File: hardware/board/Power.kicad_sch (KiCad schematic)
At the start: 34 parts

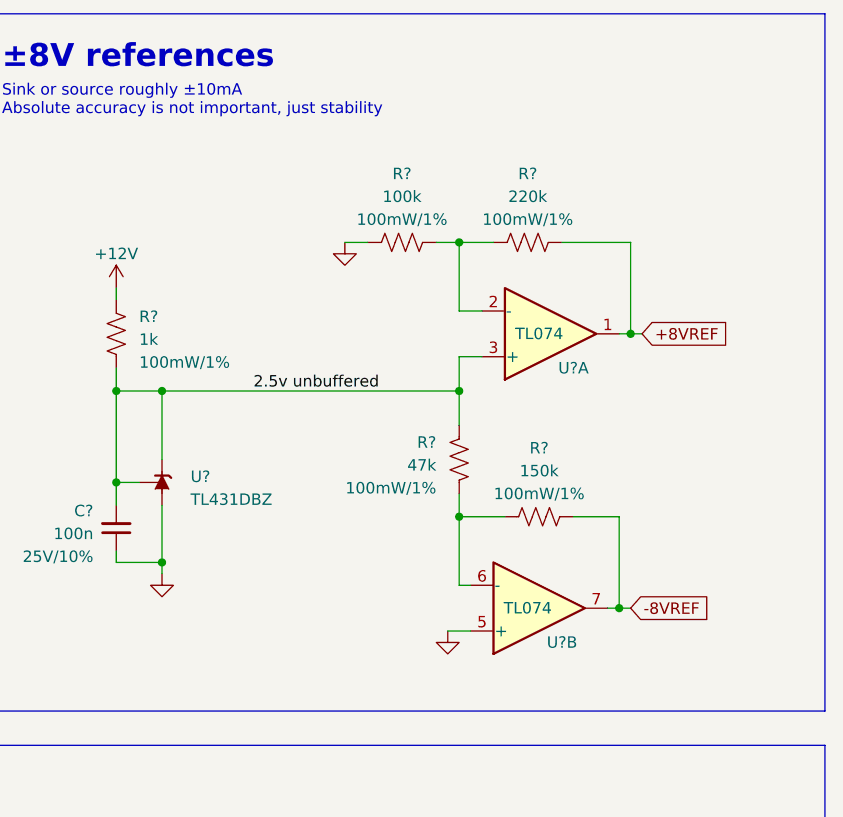
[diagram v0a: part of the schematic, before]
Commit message: Schematic getting closer to being finished
Schematic should be close to being ready to assign MPNs.
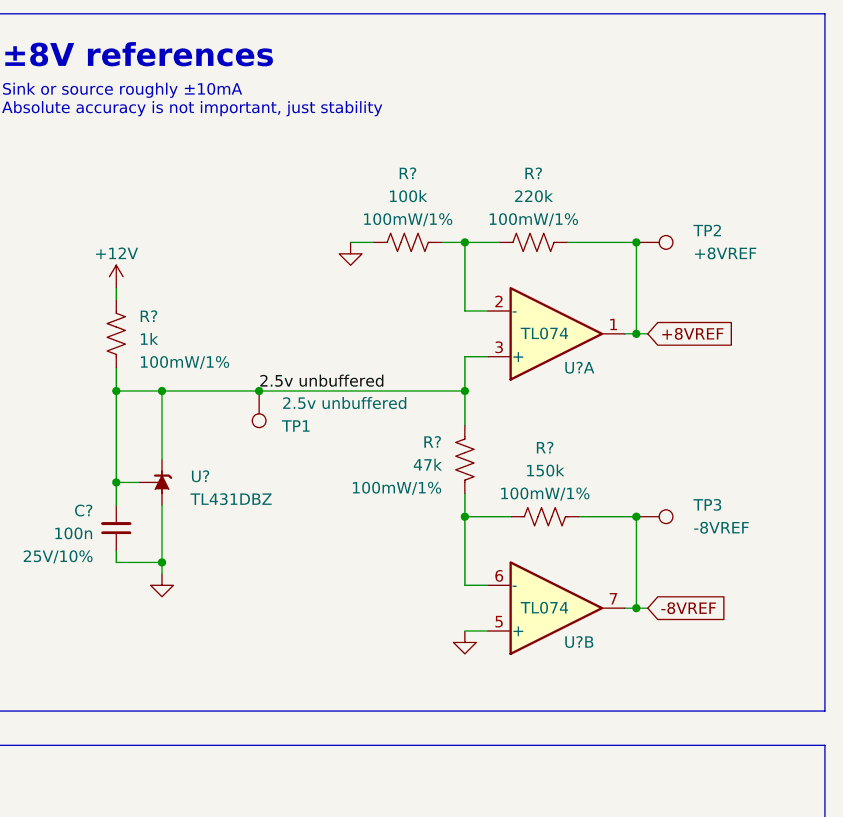
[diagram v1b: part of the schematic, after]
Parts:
- added TP1: 2.5v unbuffered, symbol Connector:TestPoint
- added TP2: +8VREF, symbol Connector:TestPoint
- added TP3: -8VREF, symbol Connector:TestPoint
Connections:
- net +8VREF: now also TP2.1
- net -8VREF: now also TP3.1
- net 2.5v unbuffered: now also TP1.1
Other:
- moved on the sheet: R?, U?A, U?B

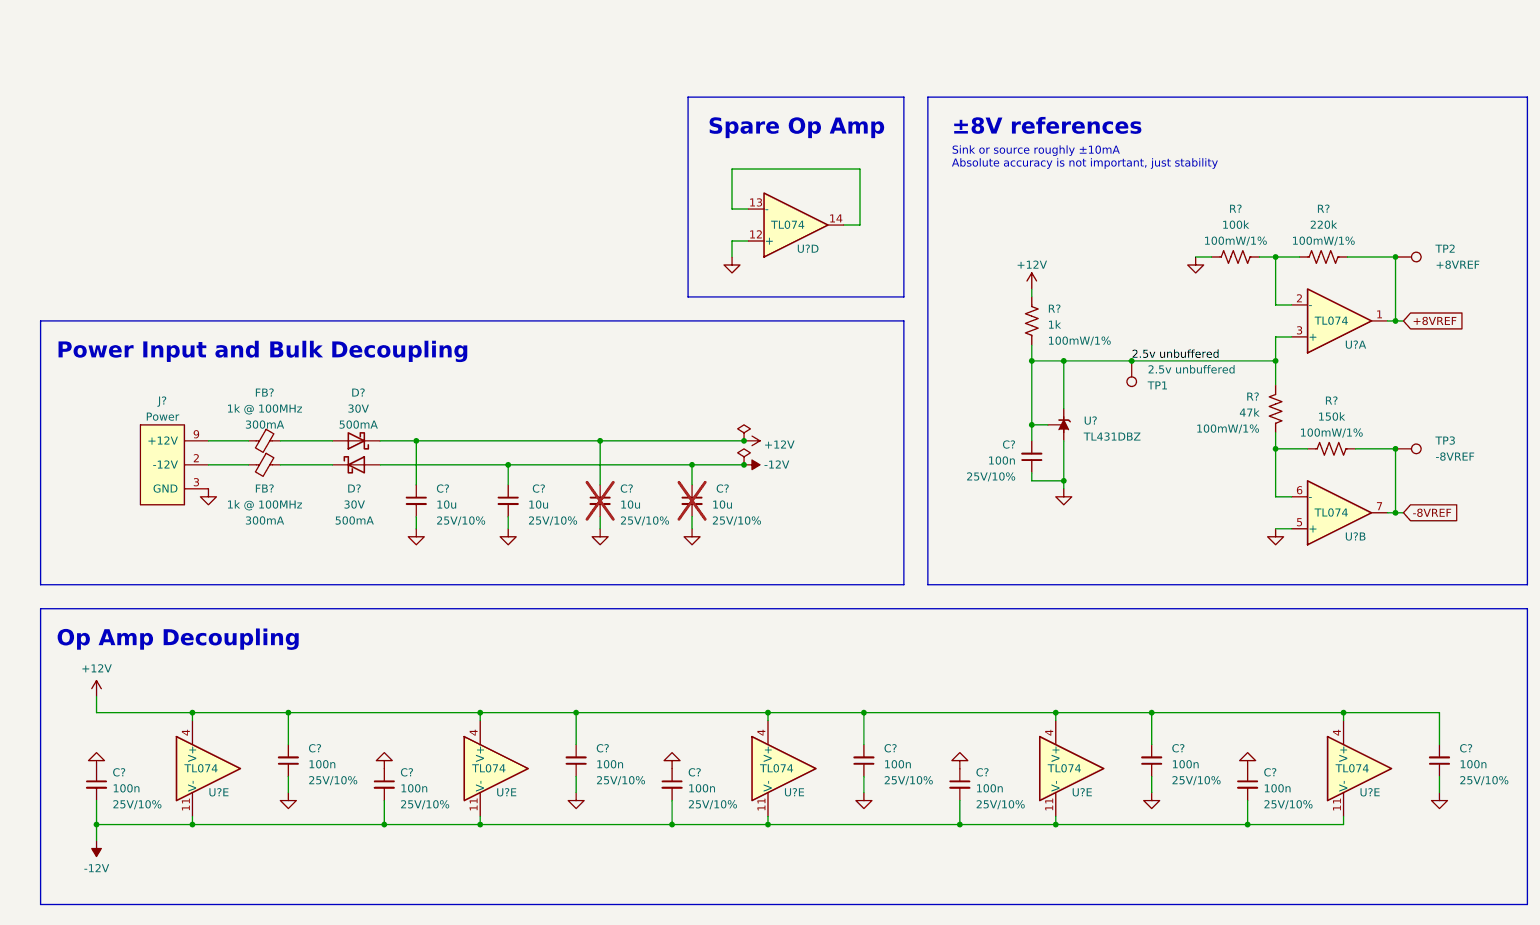
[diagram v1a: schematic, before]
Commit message: BOM Consolidation
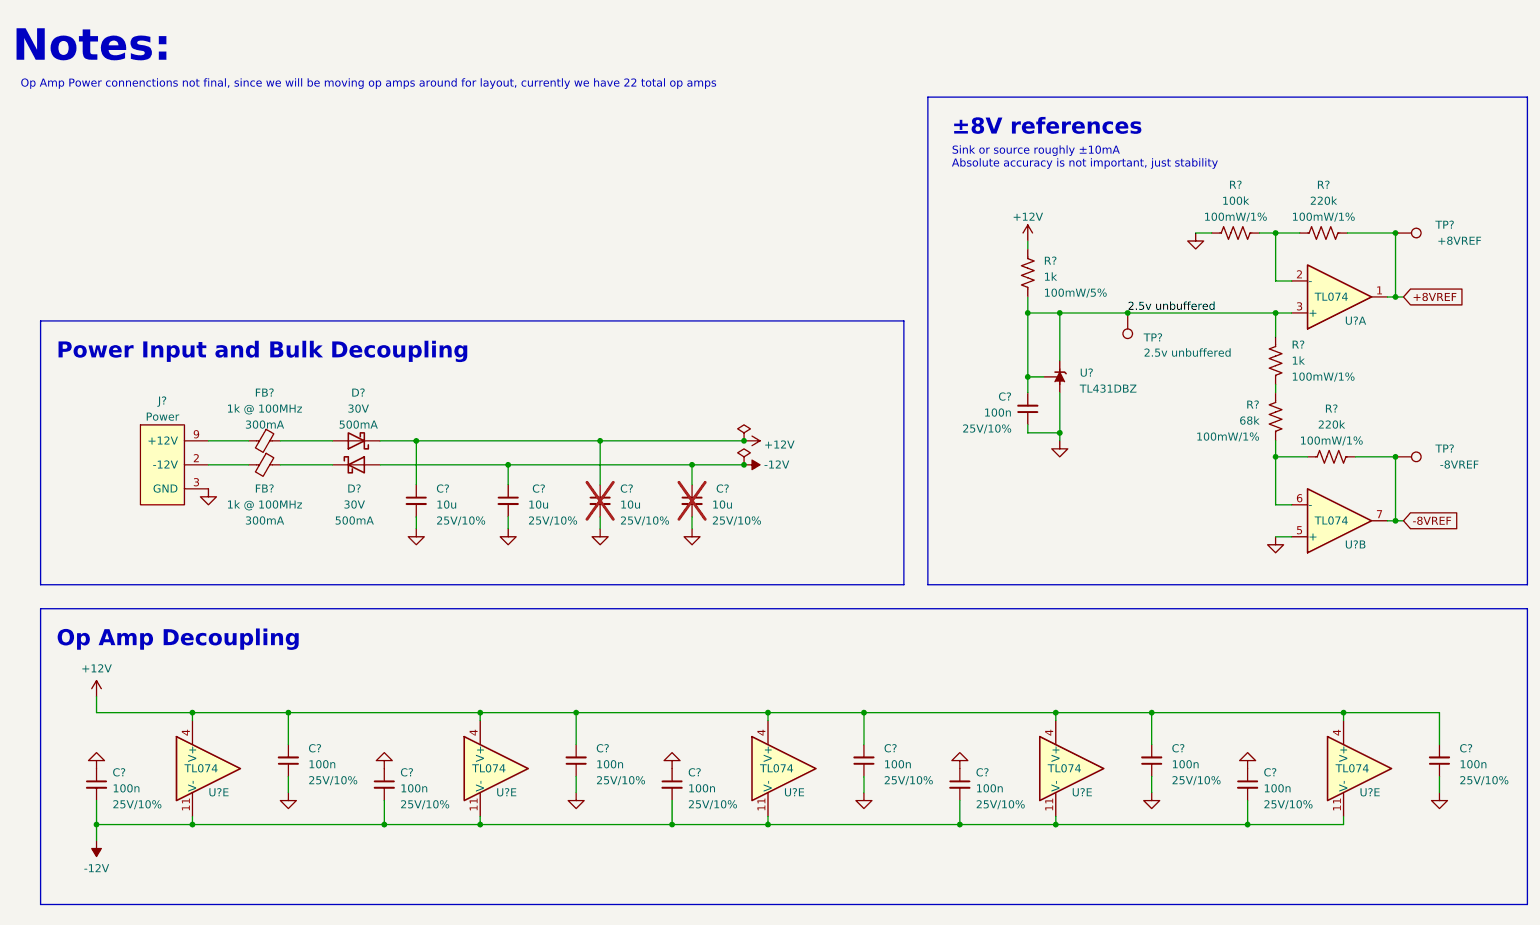
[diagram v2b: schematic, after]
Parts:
- removed U?: TL074, Package_SO:TSSOP-14_4.4x5mm_P0.65mm, symbol winterbloom:TL074
- added R?: 1k, winterbloom:R_0603_HandSolder, symbol Device:R_US
- R?: value 150k -> 220k
- R?: Rating 100mW/1% -> 100mW/5%
- R?: value 47k -> 68k
- TP?: renamed from TP3; value -8VREF -> ~; Name (none) -> -8VREF
- TP?: renamed from TP2; value +8VREF -> ~; Name (none) -> +8VREF
- TP?: renamed from TP1; value 2.5v unbuffered -> ~; Name (none) -> 2.5v unbuffered
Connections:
- net 2.5v unbuffered: now also R?.1; no longer R?.1
- new net: R?.1, R?.2
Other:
- note added: "Notes:"
- note added: "Op Amp Power connenctions not final, since we will be moving op amps around for layout, currently we have 22 total op amps"
- note removed: "Spare Op Amp"
- moved on the sheet: C?, R?, TP?, U?, U?A, U?B

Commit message: Updates for LED Drivers
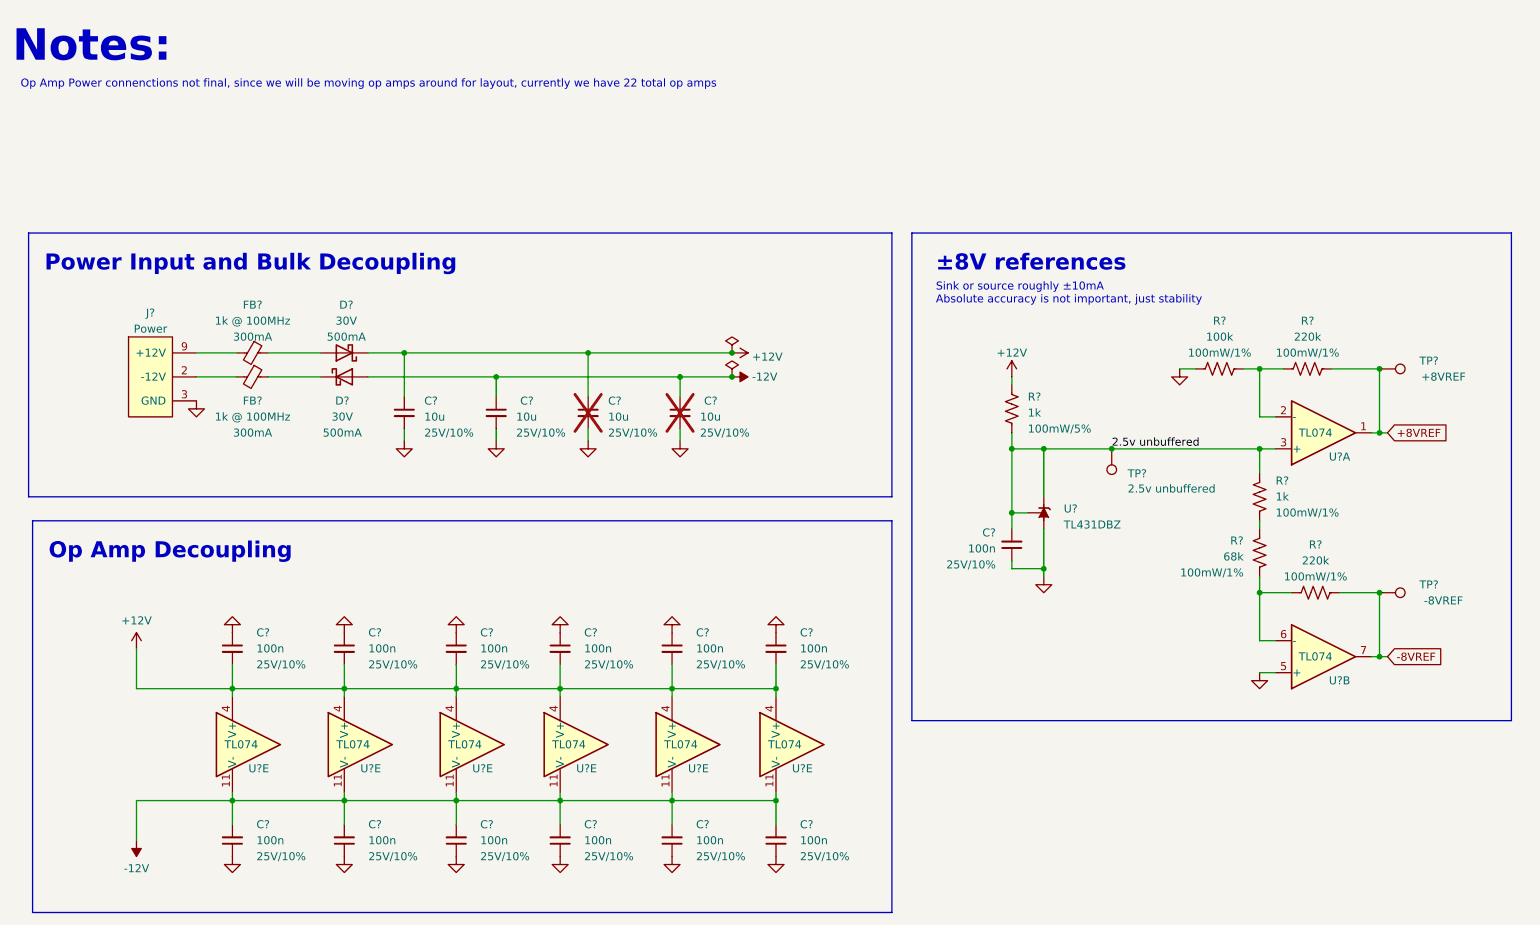
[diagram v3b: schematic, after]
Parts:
- added C? (x2): 100n, winterbloom:C_0603_HandSolder, symbol Device:C_Small
- added U?: TL074, Package_SO:TSSOP-14_4.4x5mm_P0.65mm, symbol winterbloom:TL074
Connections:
- net +12V: now also C?.2, U?.4 (V+)
- net -12V: now also C?.2, U?.11 (V-)
- net GND: now also C?.1, C?.1
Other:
- moved on the sheet: C?, D?, FB?, J?, R?, TP?, U?, U?A, U?B, U?E

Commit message: hardware: update schematic with footprints and preliminary MPNs
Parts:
- C? (x4): MPN (none) -> GRM21BR61E106KA73K; Notes 0805, 25V+, 10%, Bulk cap -> Bulk cap; mpn GRM21BR61E106KA73K -> (none); smd kit 1 -> (none)
- C? (x13): MPN (none) -> C1608X7R1E104K080AA; Notes 0603, 25V+, 10%, Bypass cap -> Bypass cap; mpn C1608X7R1E104K080AA -> (none); smd kit 1 -> (none)
- D? (x2): MPN (none) -> PMEG2005EGWX; Notes Any PMEGxxxxEGW part, 500mA If -> Power diode, any PMEGxxxxEGW part, 500mA If; mpn PMEG2005EGWX -> (none); smd kit 1 -> (none)
- FB? (x2): MPN (none) -> 742792664; mpn 742792664 -> (none); smd kit 1 -> (none)
- J?: mpn 302-S101 -> (none)
- R? (x6): smd kit 1 -> (none)
- TP201, TP202, TP203: renamed from TP?; footprint (none) -> TestPoint:TestPoint_Pad_D1.5mm
- U?: value TL431DBZ -> TL431A; LCSC C3113 -> (none); MPN (none) -> TL431BSA-7, TL431AQDBZR,215;; Rating (none) -> 1%
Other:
- title: Diode Ladder Filter -> Neptune

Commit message: Very first component layout.
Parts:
- removed U? (x2): TL074, Package_SO:TSSOP-14_4.4x5mm_P0.65mm, symbol winterbloom:TL074
- added U? (x2): TL074, Package_SO:TSSOP-14_4.4x5mm_P0.65mm, symbol winterbloom:TL074
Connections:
- net +8VREF: now also U?.8
- net -8VREF: now also U?.14
- net 2.5v unbuffered: now also U?.10 (+)
- net GND: now also U?.12 (+)
- net at R?.1, R?.2: now also U?.9 (-)
- net at R?.2, R?.2: now also U?.13 (-)

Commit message: Rough Draft of Routing Complete. Ugly but Passes DRC
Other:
- note removed: "Notes:"
- note removed: "Op Amp Power connenctions not final, since we will be moving op amps around for layout, currently we have 22 total op amps"
- moved on the sheet: C?, D?, FB?, J?, R?, TP201, TP202, TP203, U?, U?C, U?D, U?E

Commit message: Final touches before being ready for ordering
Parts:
- C? (x2): now fitted
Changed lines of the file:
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@@
   )
   (symbol (lib_id "Device:C_Small") (at 124.46 49.53 0) (unit 1)
-    (in_bom yes) (on_board yes) (dnp yes)
+    (in_bom yes) (on_board yes) (dnp no)
     (property "Reference" "C?" (at 128.27 47.6313 0)
       (effects (font (size 1.27 1.27)) (justify left))
@@
   )
   (symbol (lib_id "Device:C_Small") (at 109.855 49.53 0) (unit 1)
-    (in_bom yes) (on_board yes) (dnp yes) (fields_autoplaced)
+    (in_bom yes) (on_board yes) (dnp no) (fields_autoplaced)
     (property "Reference" "C?" (at 113.03 47.6313 0)
       (effects (font (size 1.27 1.27)) (justify left))

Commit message: hardware: minor fixes and aesthetic updates
- Fix HP LEDs being backwards
- Switch power header, pot, and jack footprints to longpad variants
- Make the text size on the front side larger
- Add "red" and "blue" text next to respective LEDs on front side
- Adjusted zone thermal spoke for better connection to GND pads
- Squished the solder jumpers for instability type closer together
- Minor adjustments to traces to accommodate longpad footprints
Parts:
- J?: footprint winterbloom:Eurorack_Power_2x5_Shrouded_Lock -> winterbloom:Eurorack_Power_2x5_Shrouded_Lock_LongPads
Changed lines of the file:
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@@
       (effects (font (size 1.27 1.27)))
     )
-    (property "Footprint" "winterbloom:Eurorack_Power_2x5_Shrouded_Lock" (at 40.005 32.385 0)
+    (property "Footprint" "winterbloom:Eurorack_Power_2x5_Shrouded_Lock_LongPads" (at 40.005 32.385 0)
       (effects (font (size 1.27 1.27)) hide)
     )
